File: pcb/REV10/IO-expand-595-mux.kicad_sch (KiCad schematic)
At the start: 53 parts, among them Q300 SI2301, Q301 SI2301, Q302 SI2301, Q303 SI2301, Q304 SI2301, Q305 SI2301, Q306 SI2301, Q307 SI2301, U402 CD4067, U404 LMV321, U501 74HC595, U502 74HC595, U503 74HCT245PW, U504 LMV324, U505 LMV324, U506 LMV321

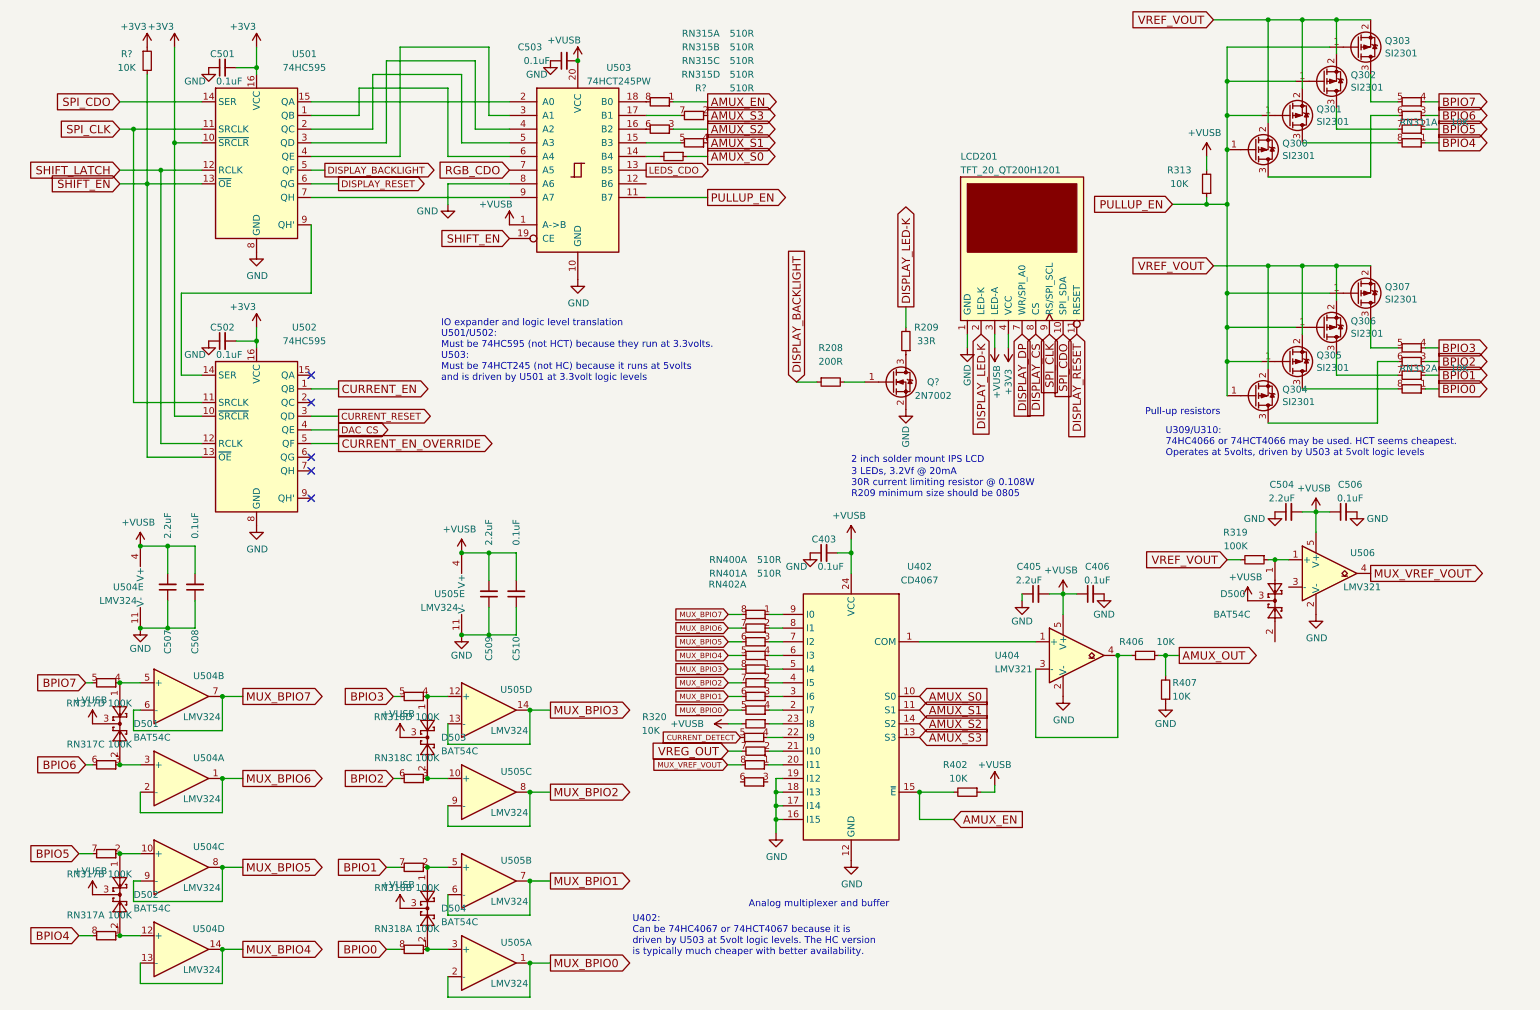
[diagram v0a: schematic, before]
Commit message: Add pulldown on VREF. Change VUSB MUX series resistor to 510R. May be other value updates that didn't get checked in previously.
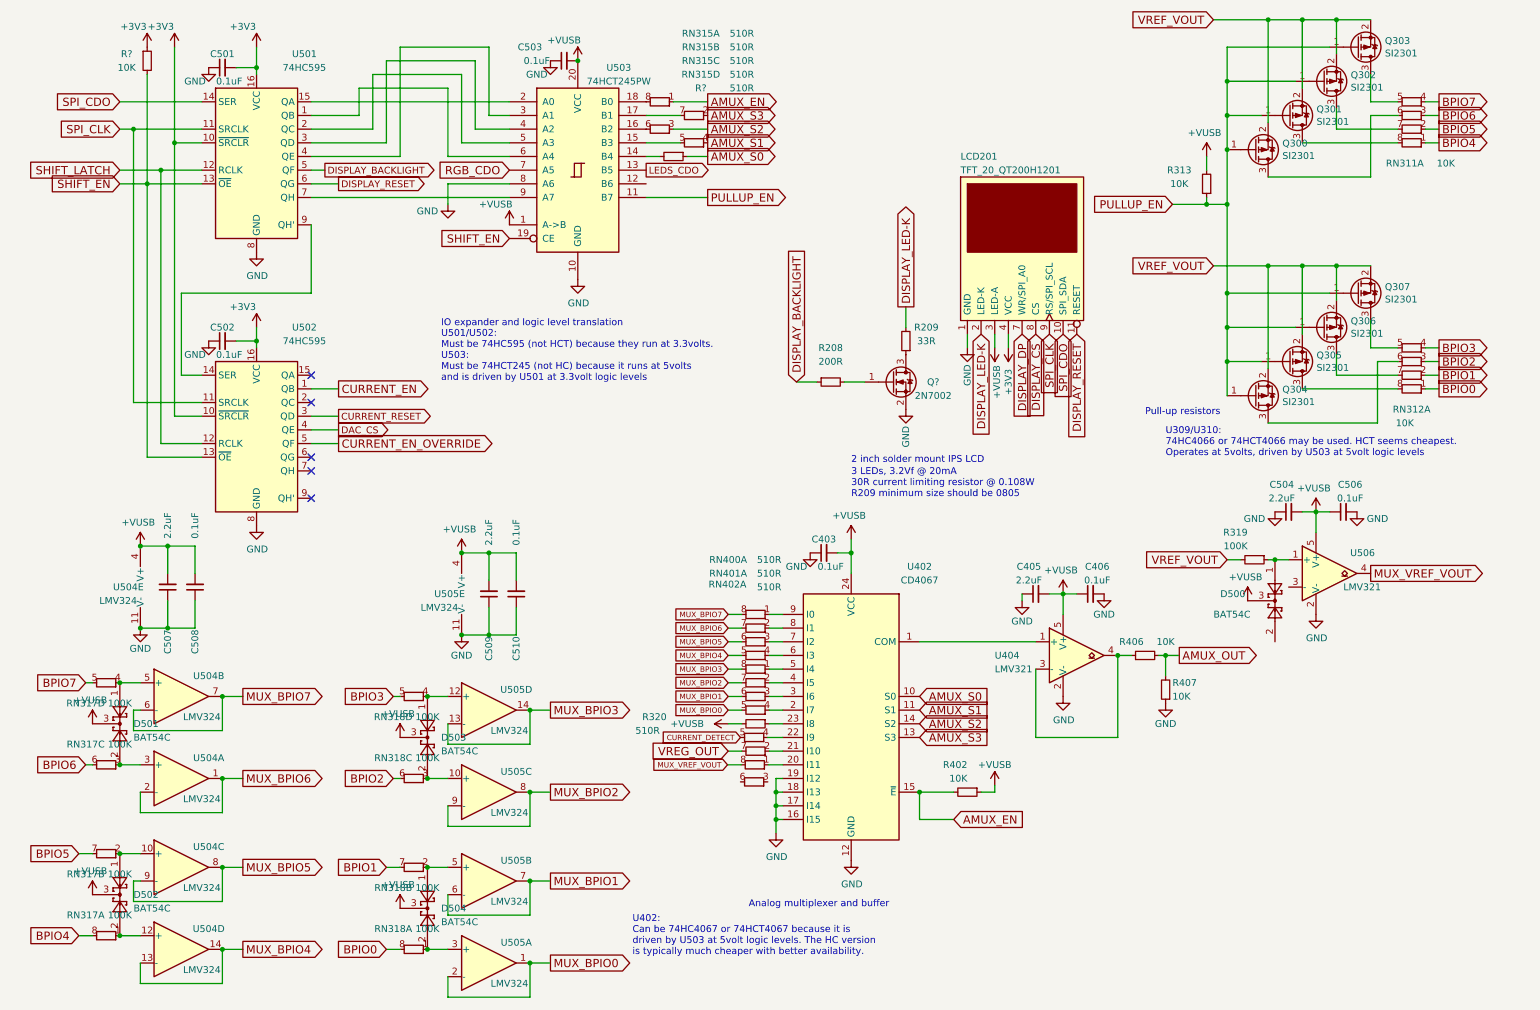
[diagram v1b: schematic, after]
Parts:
- R320: value 10K -> 510R
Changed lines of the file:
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@@
   (symbol (lib_id "dp-rarray:R_Array") (at 269.24 38.1 270) (unit 1)
     (in_bom yes) (on_board yes) (dnp no)
-    (property "Reference" "RN311" (at 270.51 34.29 90)
-      (effects (font (size 1.27 1.27)))
-    )
-    (property "Value" "10K" (at 278.13 34.29 90)
+    (property "Reference" "RN311" (at 267.97 41.91 90)
+      (effects (font (size 1.27 1.27)))
+    )
+    (property "Value" "10K" (at 275.59 41.91 90)
       (effects (font (size 1.27 1.27)))
     )
@@
   (symbol (lib_id "dp-rarray:R_Array") (at 269.24 83.82 270) (unit 1)
     (in_bom yes) (on_board yes) (dnp no)
-    (property "Reference" "RN312" (at 270.51 80.01 90)
-      (effects (font (size 1.27 1.27)))
-    )
-    (property "Value" "10K" (at 278.13 80.01 90)
+    (property "Reference" "RN312" (at 269.24 87.63 90)
+      (effects (font (size 1.27 1.27)))
+    )
+    (property "Value" "10K" (at 267.97 90.17 90)
       (effects (font (size 1.27 1.27)))
     )
@@
       (effects (font (size 1.27 1.27)) hide)
     )
-    (property "Value" "510R" (at 155.956 144.78 90)
-      (effects (font (size 1.27 1.27)) hide)
+    (property "Value" "510R" (at 149.86 120.65 90)
+      (effects (font (size 1.27 1.27)))
     )
     (property "Footprint" "Resistor_SMD:R_Array_Convex_4x0402" (at 145.796 146.558 90)
@@
       (effects (font (size 1.27 1.27)) (justify right))
     )
-    (property "Value" "10K" (at 129.54 147.32 90)
+    (property "Value" "510R" (at 129.54 147.32 90)
       (effects (font (size 1.27 1.27)) (justify right))
     )

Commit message: rev10 pcb
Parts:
- D500, D501, D502, D503, D504: value BAT54C -> BAS40-05T
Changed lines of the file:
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@@
   (symbol (lib_id "dp-rarray:R_Array") (at 83.82 140.97 270) (unit 4)
     (in_bom yes) (on_board yes) (dnp no)
-    (property "Reference" "RN318" (at 80.01 144.78 90)
-      (effects (font (size 1.27 1.27)))
-    )
-    (property "Value" "100K" (at 86.36 144.78 90)
+    (property "Reference" "RN318" (at 80.01 138.43 90)
+      (effects (font (size 1.27 1.27)))
+    )
+    (property "Value" "100K" (at 87.63 138.43 90)
       (effects (font (size 1.27 1.27)))
     )
@@
   (symbol (lib_id "Diode:BAT54C") (at 29.21 146.05 270) (unit 1)
     (in_bom yes) (on_board yes) (dnp no)
-    (property "Reference" "D501" (at 31.75 146.05 90)
-      (effects (font (size 1.27 1.27)) (justify left))
-    )
-    (property "Value" "BAT54C" (at 31.75 148.59 90)
+    (property "Reference" "D501" (at 17.78 144.78 90)
+      (effects (font (size 1.27 1.27)) (justify left))
+    )
+    (property "Value" "BAS40-05T" (at 16.51 147.32 90)
       (effects (font (size 1.27 1.27)) (justify left))
     )
@@
   (symbol (lib_id "dp-rarray:R_Array") (at 26.67 153.67 270) (unit 3)
     (in_bom yes) (on_board yes) (dnp no)
-    (property "Reference" "RN317" (at 22.86 149.86 90)
-      (effects (font (size 1.27 1.27)))
-    )
-    (property "Value" "100K" (at 29.21 149.86 90)
+    (property "Reference" "RN317" (at 21.59 157.48 90)
+      (effects (font (size 1.27 1.27)))
+    )
+    (property "Value" "100K" (at 29.21 157.48 90)
       (effects (font (size 1.27 1.27)))
     )
@@
   (symbol (lib_id "Diode:BAT54C") (at 243.84 123.19 270) (unit 1)
     (in_bom yes) (on_board yes) (dnp no)
-    (property "Reference" "D500" (at 233.68 121.92 90)
-      (effects (font (size 1.27 1.27)) (justify left))
-    )
-    (property "Value" "BAT54C" (at 232.41 125.73 90)
+    (property "Reference" "D500" (at 232.41 123.19 90)
+      (effects (font (size 1.27 1.27)) (justify left))
+    )
+    (property "Value" "BAS40-05T" (at 232.41 125.73 90)
       (effects (font (size 1.27 1.27)) (justify left))
     )
@@
   (symbol (lib_id "Diode:BAT54C") (at 86.36 148.59 270) (unit 1)
     (in_bom yes) (on_board yes) (dnp no)
-    (property "Reference" "D503" (at 88.9 148.59 90)
-      (effects (font (size 1.27 1.27)) (justify left))
-    )
-    (property "Value" "BAT54C" (at 88.9 151.13 90)
+    (property "Reference" "D503" (at 74.93 147.32 90)
+      (effects (font (size 1.27 1.27)) (justify left))
+    )
+    (property "Value" "BAS40-05T" (at 74.93 149.86 90)
       (effects (font (size 1.27 1.27)) (justify left))
     )
@@
   (symbol (lib_id "dp-rarray:R_Array") (at 83.82 156.21 270) (unit 3)
     (in_bom yes) (on_board yes) (dnp no)
-    (property "Reference" "RN318" (at 80.01 152.4 90)
-      (effects (font (size 1.27 1.27)))
-    )
-    (property "Value" "100K" (at 86.36 152.4 90)
+    (property "Reference" "RN318" (at 80.01 158.75 90)
+      (effects (font (size 1.27 1.27)))
+    )
+    (property "Value" "100K" (at 86.36 158.75 90)
       (effects (font (size 1.27 1.27)))
     )
@@
   (symbol (lib_id "dp-rarray:R_Array") (at 26.67 185.42 270) (unit 1)
     (in_bom yes) (on_board yes) (dnp no)
-    (property "Reference" "RN317" (at 22.86 181.61 90)
-      (effects (font (size 1.27 1.27)))
-    )
-    (property "Value" "100K" (at 29.21 181.61 90)
+    (property "Reference" "RN317" (at 21.59 189.23 90)
+      (effects (font (size 1.27 1.27)))
+    )
+    (property "Value" "100K" (at 29.21 189.23 90)
       (effects (font (size 1.27 1.27)))
     )
@@
   (symbol (lib_id "Device:R_Small") (at 240.03 115.57 270) (unit 1)
     (in_bom yes) (on_board yes) (dnp no)
-    (property "Reference" "R319" (at 238.76 110.49 90)
+    (property "Reference" "R319" (at 238.76 113.03 90)
       (effects (font (size 1.27 1.27)) (justify right))
     )
-    (property "Value" "100K" (at 238.76 113.03 90)
+    (property "Value" "100K" (at 245.11 113.03 90)
       (effects (font (size 1.27 1.27)) (justify right))
     )
@@
   (symbol (lib_id "Diode:BAT54C") (at 29.21 177.8 270) (unit 1)
     (in_bom yes) (on_board yes) (dnp no)
-    (property "Reference" "D502" (at 31.75 177.8 90)
-      (effects (font (size 1.27 1.27)) (justify left))
-    )
-    (property "Value" "BAT54C" (at 31.75 180.34 90)
+    (property "Reference" "D502" (at 17.78 176.53 90)
+      (effects (font (size 1.27 1.27)) (justify left))
+    )
+    (property "Value" "BAS40-05T" (at 17.78 179.07 90)
       (effects (font (size 1.27 1.27)) (justify left))
     )
@@
   (symbol (lib_id "dp-rarray:R_Array") (at 83.82 172.72 270) (unit 2)
     (in_bom yes) (on_board yes) (dnp no)
-    (property "Reference" "RN318" (at 80.01 176.53 90)
-      (effects (font (size 1.27 1.27)))
-    )
-    (property "Value" "100K" (at 86.36 176.53 90)
+    (property "Reference" "RN318" (at 78.74 170.18 90)
+      (effects (font (size 1.27 1.27)))
+    )
+    (property "Value" "100K" (at 86.36 170.18 90)
       (effects (font (size 1.27 1.27)))
     )
@@
   (symbol (lib_id "Diode:BAT54C") (at 86.36 180.34 270) (unit 1)
     (in_bom yes) (on_board yes) (dnp no)
-    (property "Reference" "D504" (at 88.9 180.34 90)
-      (effects (font (size 1.27 1.27)) (justify left))
-    )
-    (property "Value" "BAT54C" (at 88.9 182.88 90)
+    (property "Reference" "D504" (at 74.93 179.07 90)
+      (effects (font (size 1.27 1.27)) (justify left))
+    )
+    (property "Value" "BAS40-05T" (at 74.93 181.61 90)
       (effects (font (size 1.27 1.27)) (justify left))
     )
@@
   (symbol (lib_id "dp-rarray:R_Array") (at 83.82 187.96 270) (unit 1)
     (in_bom yes) (on_board yes) (dnp no)
-    (property "Reference" "RN318" (at 80.01 184.15 90)
-      (effects (font (size 1.27 1.27)))
-    )
-    (property "Value" "100K" (at 86.36 184.15 90)
+    (property "Reference" "RN318" (at 78.74 191.77 90)
+      (effects (font (size 1.27 1.27)))
+    )
+    (property "Value" "100K" (at 86.36 191.77 90)
       (effects (font (size 1.27 1.27)))
     )
@@
   (symbol (lib_id "dp-rarray:R_Array") (at 26.67 170.18 270) (unit 2)
     (in_bom yes) (on_board yes) (dnp no)
-    (property "Reference" "RN317" (at 22.86 173.99 90)
-      (effects (font (size 1.27 1.27)))
-    )
-    (property "Value" "100K" (at 29.21 173.99 90)
+    (property "Reference" "RN317" (at 21.59 167.64 90)
+      (effects (font (size 1.27 1.27)))
+    )
+    (property "Value" "100K" (at 29.21 167.64 90)
       (effects (font (size 1.27 1.27)))
     )
@@
   (symbol (lib_id "dp-rarray:R_Array") (at 26.67 138.43 270) (unit 4)
     (in_bom yes) (on_board yes) (dnp no)
-    (property "Reference" "RN317" (at 22.86 142.24 90)
-      (effects (font (size 1.27 1.27)))
-    )
-    (property "Value" "100K" (at 29.21 142.24 90)
+    (property "Reference" "RN317" (at 21.59 135.89 90)
+      (effects (font (size 1.27 1.27)))
+    )
+    (property "Value" "100K" (at 29.21 135.89 90)
       (effects (font (size 1.27 1.27)))
     )
@@
       (effects (font (size 1.27 1.27)) hide)
     )
-    (property "Value" "+VUSB" (at 23.749 141.6558 0)
-      (effects (font (size 1.27 1.27)))
-    )
+    (property "Value" "+VUSB" (at 24.13 142.24 0)
+      (effects (font (size 1.27 1.27)))
+    )

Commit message: schematic cleanup
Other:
- note added: "IO pin/analog MUX buffer"
- note removed: "U309/U310: 74HC4066 or 74HCT4066 may be used. HCT seems cheapest. Operates at 5volts, driven by U503 at 5volt logic levels"
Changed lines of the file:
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@@
+    (effects (font (size 1.27 1.27)) (justify left bottom))
+  )
+  (text "IO pin/analog MUX buffer" (at 55.88 196.85 0)
     (effects (font (size 1.27 1.27)) (justify left bottom))
   )
@@
     (effects (font (size 1.27 1.27)) (justify left bottom))
   )
-  (text "U309/U310:\n74HC4066 or 74HCT4066 may be used. HCT seems cheapest.\nOperates at 5volts, driven by U503 at 5volt logic levels"
-    (at 223.52 96.52 0)
+  (text "Pull-up resistors" (at 245.11 93.98 0)
     (effects (font (size 1.27 1.27)) (justify left bottom))
   )
-  (text "Pull-up resistors" (at 219.71 88.9 0)
-    (effects (font (size 1.27 1.27)) (justify left bottom))
-  )
